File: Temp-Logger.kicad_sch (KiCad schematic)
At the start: 0 parts

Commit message: Added subsheet ports and a placeholder mcu
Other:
- added sheet Microcontroller (microcontroller.kicad_sch)
- added sheet Temperature Sensor (temp_sense.kicad_sch)
- added sheet Transciever (transciever.kicad_sch)
- company: (none) -> UVM SEED Team 512 - NWTL
- title: (none) -> Temperature Logger

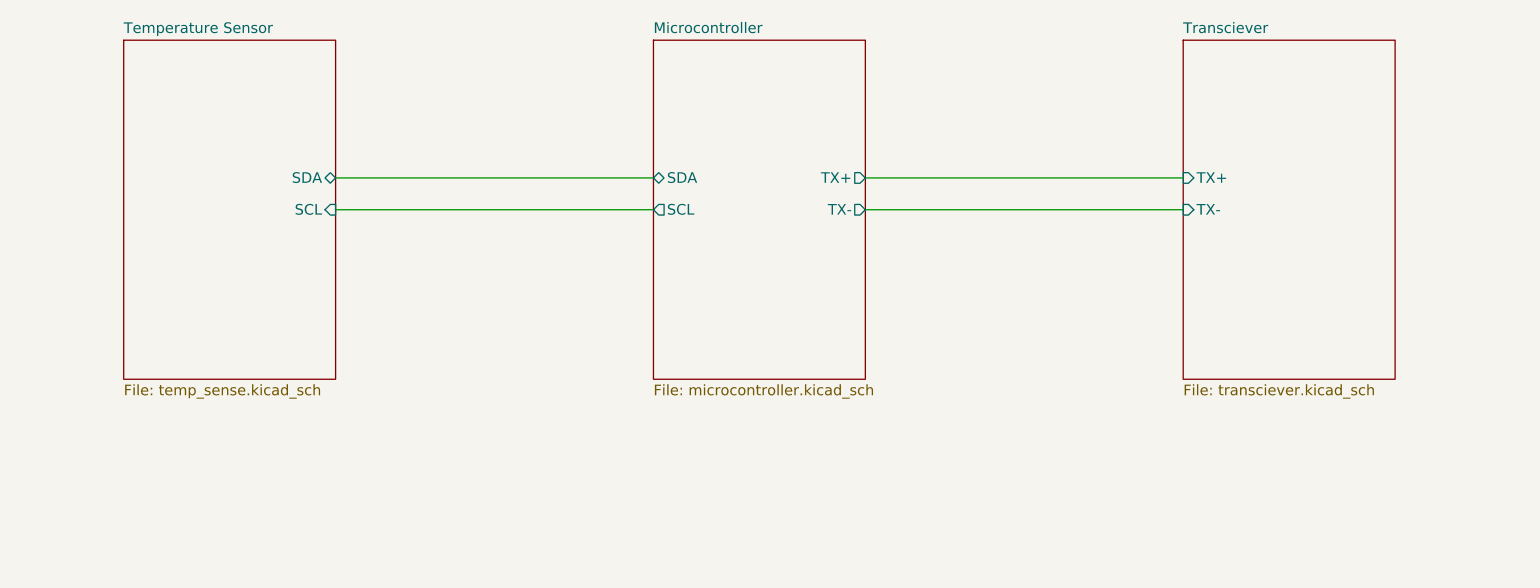
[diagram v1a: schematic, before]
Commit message: Created new hierarchy, added new nRF MCU, started really digging into schematic
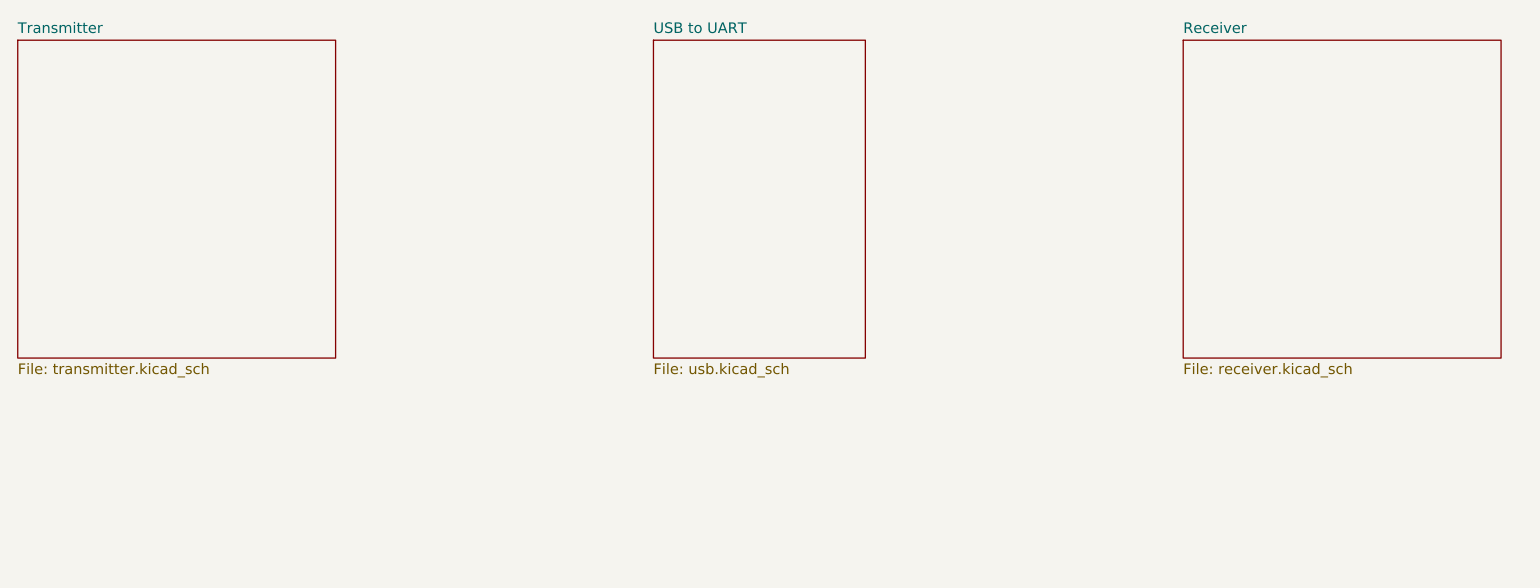
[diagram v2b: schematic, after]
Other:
- removed sheet Microcontroller
- removed sheet Temperature Sensor
- removed sheet Transciever
- added sheet Receiver (receiver.kicad_sch)
- added sheet Transmitter (transmitter.kicad_sch)
- added sheet USB to UART (usb.kicad_sch)
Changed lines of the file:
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@@
 		(company "UVM SEED Team 512 - NWTL")
 	)
-	(wire
-		(pts
-			(xy 101.6 96.52) (xy 139.7 96.52)
-		)
-		(stroke
-			(width 0)
-			(type default)
-		)
-	)
-	(wire
-		(pts
-			(xy 101.6 92.71) (xy 139.7 92.71)
-		)
-		(stroke
-			(width 0)
-			(type default)
-		)
-	)
-	(wire
-		(pts
-			(xy 165.1 96.52) (xy 203.2 96.52)
-		)
-		(stroke
-			(width 0)
-			(type default)
-		)
-	)
-	(wire
-		(pts
-			(xy 165.1 92.71) (xy 203.2 92.71)
-		)
-		(stroke
-			(width 0)
-			(type default)
-		)
-	)
 	(sheet
-		(at 76.2 76.2)
-		(size 25.4 40.64)
+		(at 203.2 76.2)
+		(size 38.1 38.1)
 		(exclude_from_sim no)
 		(in_bom yes)
@@
 			(color 0 0 0 0)
 		)
-		(property "Sheetname" "Temperature Sensor"
-			(at 76.2 75.4884 0)
+		(property "Sheetname" "Receiver"
+			(at 203.2 75.4884 0)
 			(show_name no)
 			(do_not_autoplace no)
@@
 			)
 		)
-		(property "Sheetfile" "temp_sense.kicad_sch"
-			(at 76.2 117.4246 0)
+		(property "Sheetfile" "receiver.kicad_sch"
+			(at 203.2 114.8846 0)
 			(show_name no)
 			(do_not_autoplace no)
@@
 			)
 		)
-		(pin "SCL" input
-			(at 101.6 96.52 0)
-			(effects
-				(font
-					(size 1.27 1.27)
-				)
-				(justify right)
-			)
-		)
-		(pin "SDA" bidirectional
-			(at 101.6 92.71 0)
-			(effects
-				(font
-					(size 1.27 1.27)
-				)
-				(justify right)
-			)
-		)
 		(instances
 			(project "Temp-Logger"
 				(path "/9c5f4d5b-9930-4cae-a7d7-03685cadac72"
-					(page "2")
+					(page "3")
 				)
 			)
@@
 	(sheet
 		(at 139.7 76.2)
-		(size 25.4 40.64)
+		(size 25.4 38.1)
 		(exclude_from_sim no)
 		(in_bom yes)
@@
 			(color 0 0 0 0)
 		)
-		(property "Sheetname" "Microcontroller"
+		(property "Sheetname" "USB to UART"
 			(at 139.7 75.4884 0)
 			(show_name no)
@@
 			)
 		)
-		(property "Sheetfile" "microcontroller.kicad_sch"
-			(at 139.7 117.4246 0)
+		(property "Sheetfile" "usb.kicad_sch"
+			(at 139.7 114.8846 0)
 			(show_name no)
 			(do_not_autoplace no)
@@
 			)
 		)
-		(pin "TX-" output
-			(at 165.1 96.52 0)
-			(effects
-				(font
-					(size 1.27 1.27)
-				)
-				(justify right)
-			)
-		)
-		(pin "TX+" output
-			(at 165.1 92.71 0)
-			(effects
-				(font
-					(size 1.27 1.27)
-				)
-				(justify right)
-			)
-		)
-		(pin "SCL" output
-			(at 139.7 96.52 180)
-			(effects
-				(font
-					(size 1.27 1.27)
-				)
-				(justify left)
-			)
-		)
-		(pin "SDA" bidirectional
-			(at 139.7 92.71 180)
-			(effects
-				(font
-					(size 1.27 1.27)
-				)
-				(justify left)
-			)
-		)
 		(instances
 			(project "Temp-Logger"
 				(path "/9c5f4d5b-9930-4cae-a7d7-03685cadac72"
-					(page "3")
+					(page "8")
 				)
 			)
@@
 	)
 	(sheet
-		(at 203.2 76.2)
-		(size 25.4 40.64)
+		(at 63.5 76.2)
+		(size 38.1 38.1)
 		(exclude_from_sim no)
 		(in_bom yes)
@@
 			(color 0 0 0 0)
 		)
-		(property "Sheetname" "Transciever"
-			(at 203.2 75.4884 0)
+		(property "Sheetname" "Transmitter"
+			(at 63.5 75.4884 0)
 			(show_name no)
 			(do_not_autoplace no)
@@
 			)
 		)
-		(property "Sheetfile" "transciever.kicad_sch"
-			(at 203.2 117.4246 0)
+		(property "Sheetfile" "transmitter.kicad_sch"
+			(at 63.5 114.8846 0)
 			(show_name no)
 			(do_not_autoplace no)
@@
 			)
 		)
-		(pin "TX-" input
-			(at 203.2 96.52 180)
-			(effects
-				(font
-					(size 1.27 1.27)
-				)
-				(justify left)
-			)
-		)
-		(pin "TX+" input
-			(at 203.2 92.71 180)
-			(effects
-				(font
-					(size 1.27 1.27)
-				)
-				(justify left)
-			)
-		)
 		(instances
 			(project "Temp-Logger"
 				(path "/9c5f4d5b-9930-4cae-a7d7-03685cadac72"
-					(page "4")
+					(page "2")
 				)
 			)

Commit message: Added USB to UART circuitry, cleaned up top sheets, added more supporting circuitry for TX MCU
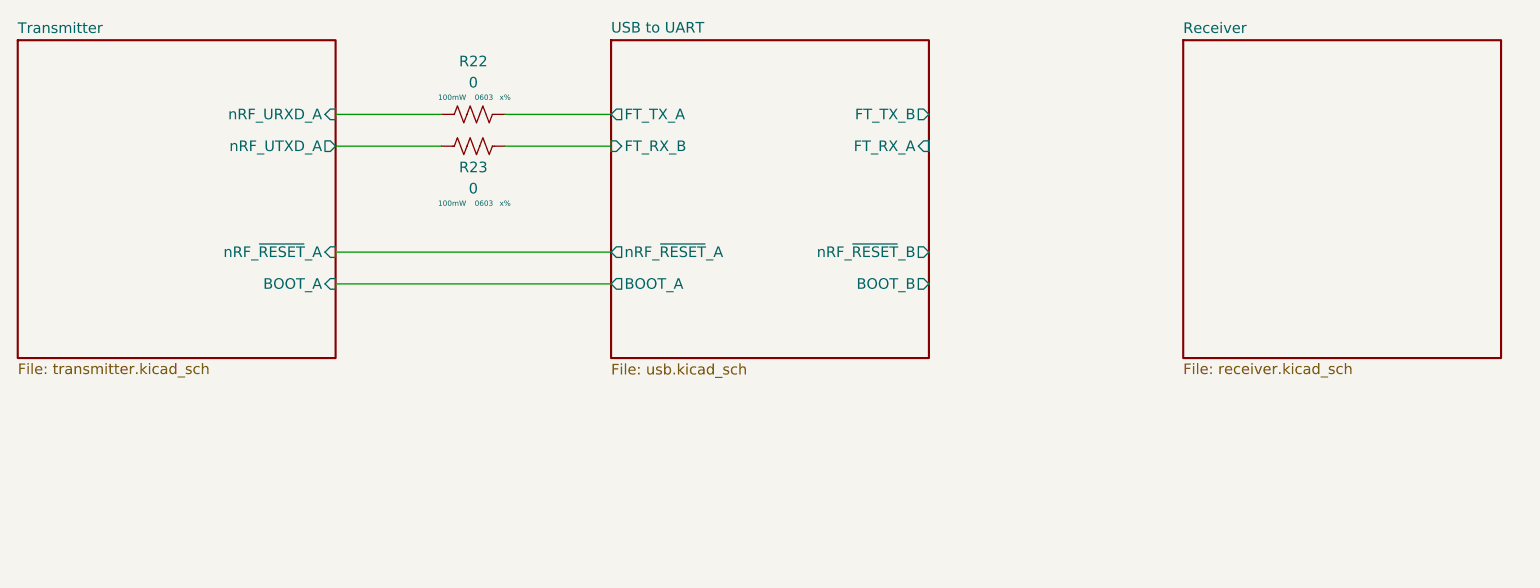
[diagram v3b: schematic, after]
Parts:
- added R22, R23: 0, Resistor_SMD:R_0603_1608Metric_Pad0.98x0.95mm_HandSolder, symbol AERO_Resistors:R_0603
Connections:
- new net Transmitter/nRF_URXD_A: R22.1
- new net Transmitter/nRF_UTXD_A: R23.1
- new net USB to UART/FT_RX_B: R23.2
- new net USB to UART/FT_TX_A: R22.2
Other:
- sheet Transmitter ports: added BOOT_A, nRF_URXD_A, nRF_UTXD_A, nRF_~{RESET}_A; removed none
- sheet USB to UART ports: added BOOT_A, BOOT_B, FT_RX_A, FT_RX_B, FT_TX_A, FT_TX_B, nRF_~{RESET}_A, nRF_~{RESET}_B; removed none

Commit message: Finished schematic, added power section for external power (both power supply and battery), added current sensing for TX microcontroller
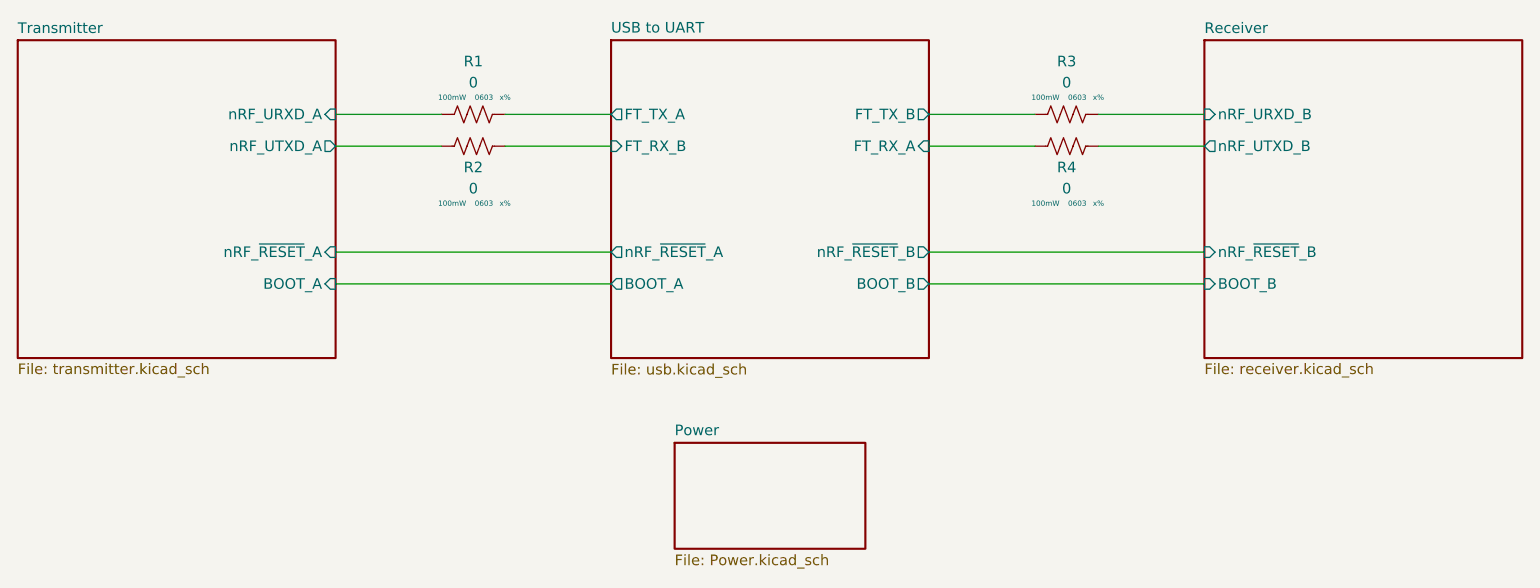
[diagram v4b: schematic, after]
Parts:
- added R3, R4: 0, Resistor_SMD:R_0603_1608Metric_Pad0.98x0.95mm_HandSolder, symbol AERO_Resistors:R_0603
- renumbered R22 to R1, R23 to R2
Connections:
- net USB to UART/FT_RX_A: now also R4.1
- net USB to UART/FT_TX_B: now also R3.1
- new net Receiver/nRF_URXD_B: R3.2
- new net Receiver/nRF_UTXD_B: R4.2
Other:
- added sheet Power (Power.kicad_sch)
- sheet Receiver ports: added BOOT_B, nRF_URXD_B, nRF_UTXD_B, nRF_~{RESET}_B; removed none

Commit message: Made most capacitors 0402 for mcu sheets, defined board shape and started layout
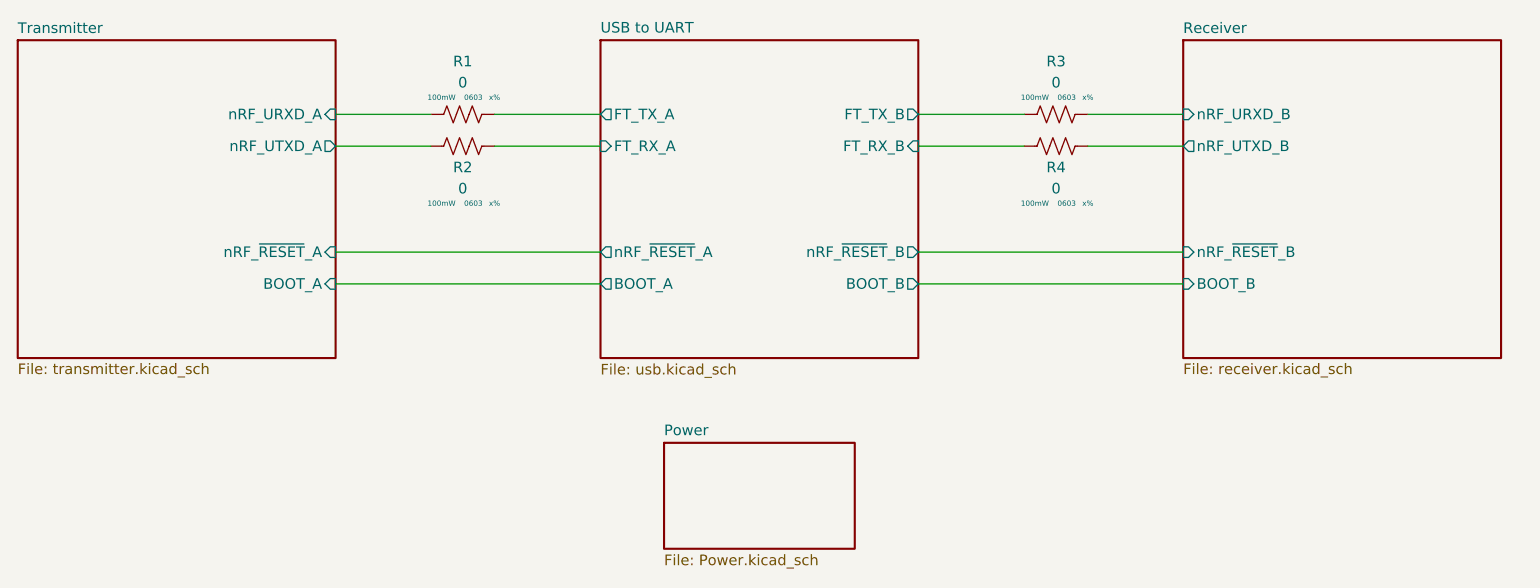
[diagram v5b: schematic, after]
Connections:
- net USB to UART/FT_RX_A: now also R2.2; no longer R4.1
- net USB to UART/FT_RX_B: now also R4.1; no longer R2.2
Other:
- moved on the sheet: R1, R2, R3, R4
